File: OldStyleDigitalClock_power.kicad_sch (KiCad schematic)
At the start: 23 parts, among them J1 USB_C_IN, J2 USB_A_OUT, J3 USB_A_OUT, U14 NA555P

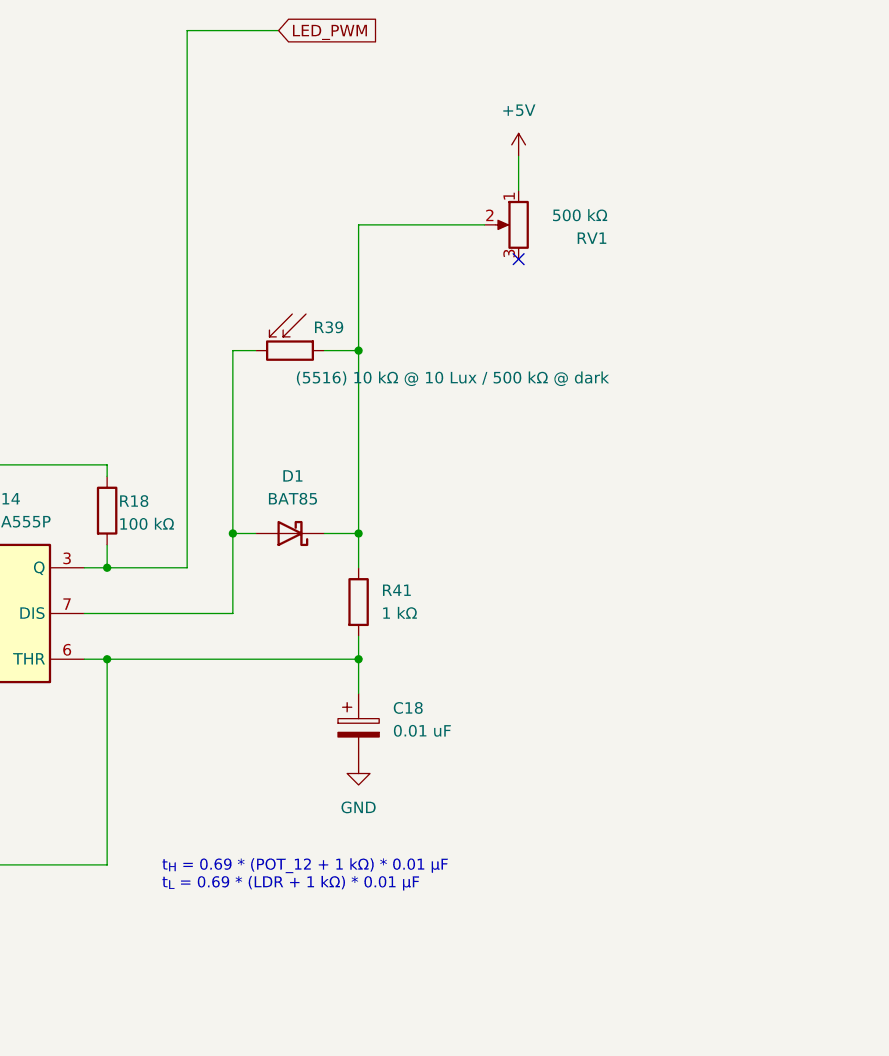
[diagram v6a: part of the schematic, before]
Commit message: Increased C18 value
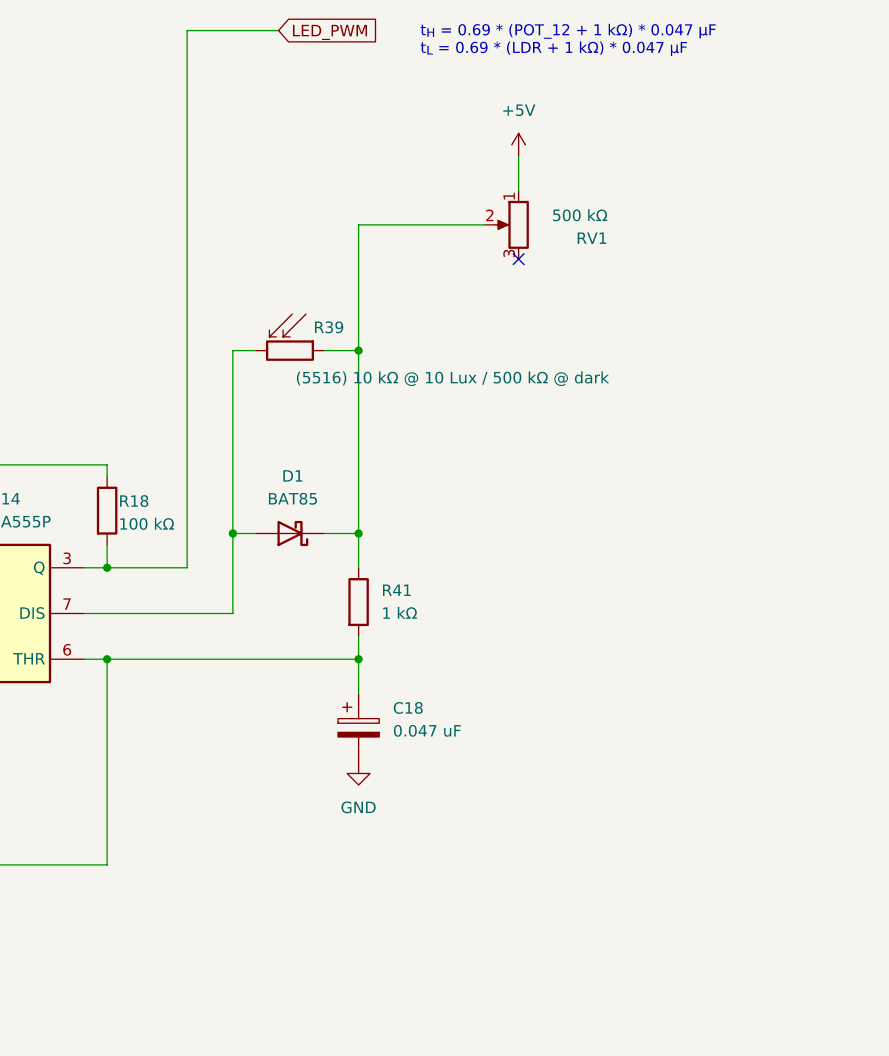
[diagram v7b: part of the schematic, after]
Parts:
- C18: value 0.01 uF -> 0.047 uF
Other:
- note added: "t_{H} = 0.69 * (POT_12 + 1 kΩ) * 0.047 µF t_{L} = 0.69 * (LDR + 1 kΩ) * 0.047 µF"
- note removed: "t_{H} = 0.69 * (POT_12 + 1 kΩ) * 0.01 µF t_{L} = 0.69 * (LDR + 1 kΩ) * 0.01 µF"
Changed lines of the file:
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@@
 		(company "Pasquale Lafiosca")
 	)
-	(text "t_{H} = 0.69 * (POT_12 + 1 kΩ) * 0.01 µF\nt_{L} = 0.69 * (LDR + 1 kΩ) * 0.01 µF\n\n"
+	(text "t_{H} = 0.69 * (POT_12 + 1 kΩ) * 0.047 µF\nt_{L} = 0.69 * (LDR + 1 kΩ) * 0.047 µF\n\n"
 		(exclude_from_sim no)
-		(at 211.836 111.252 0)
+		(at 240.538 18.542 0)
 		(effects
 			(font
@@
 			)
 		)
-		(property "Value" "0.01 uF"
+		(property "Value" "0.047 uF"
 			(at 237.49 96.9009 0)
 			(effects

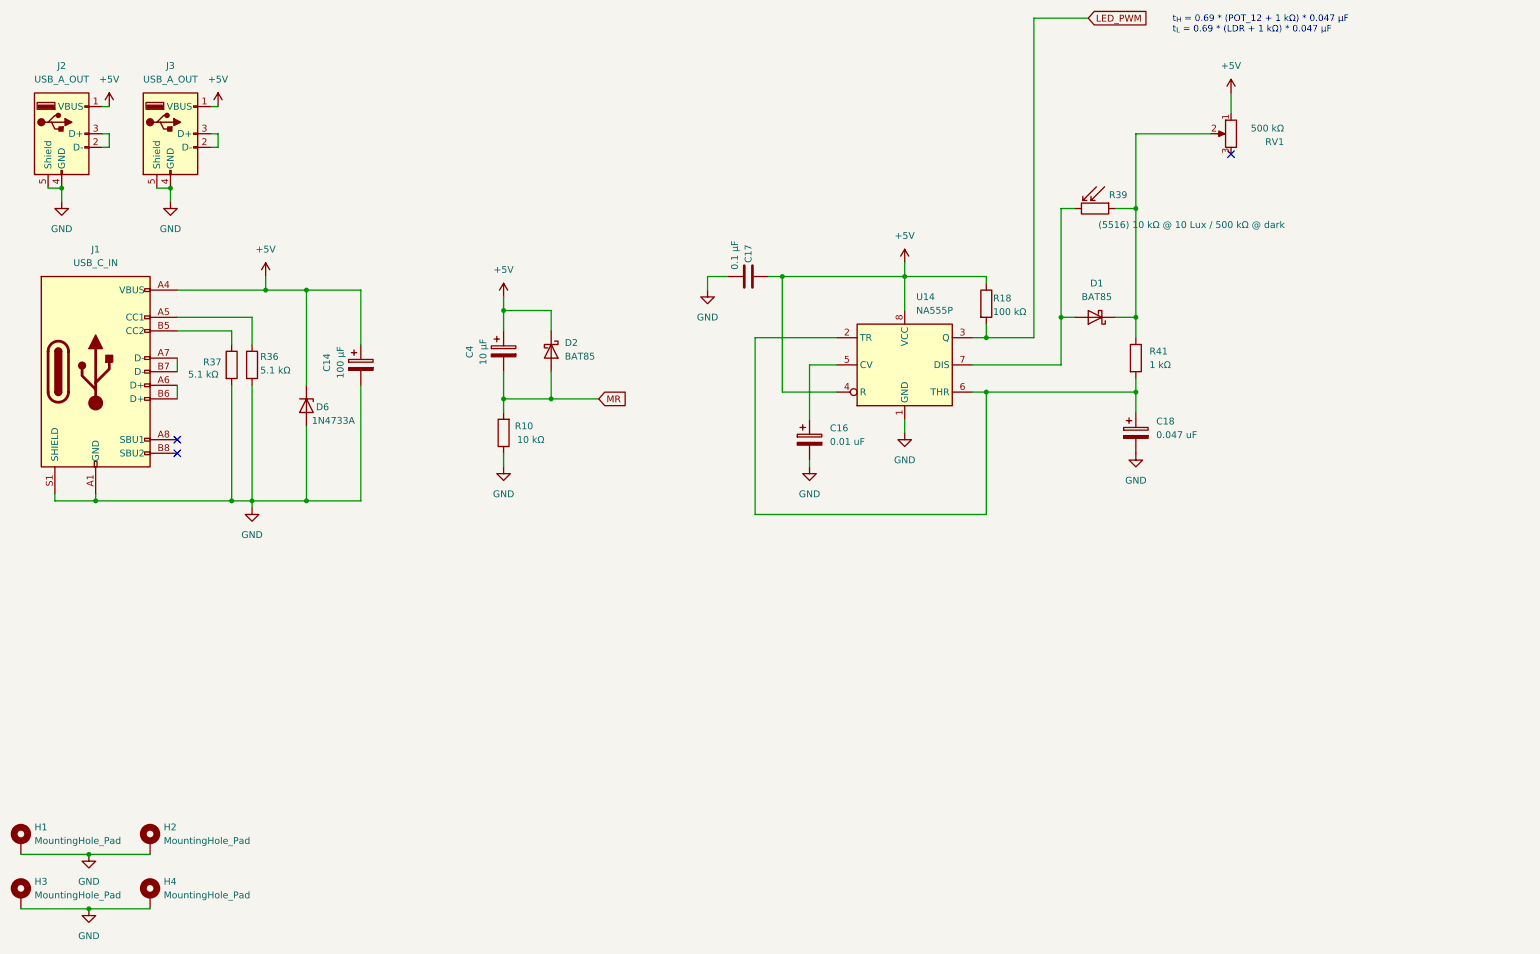
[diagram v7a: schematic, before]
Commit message: Partial commit: Moved to SMD footprints
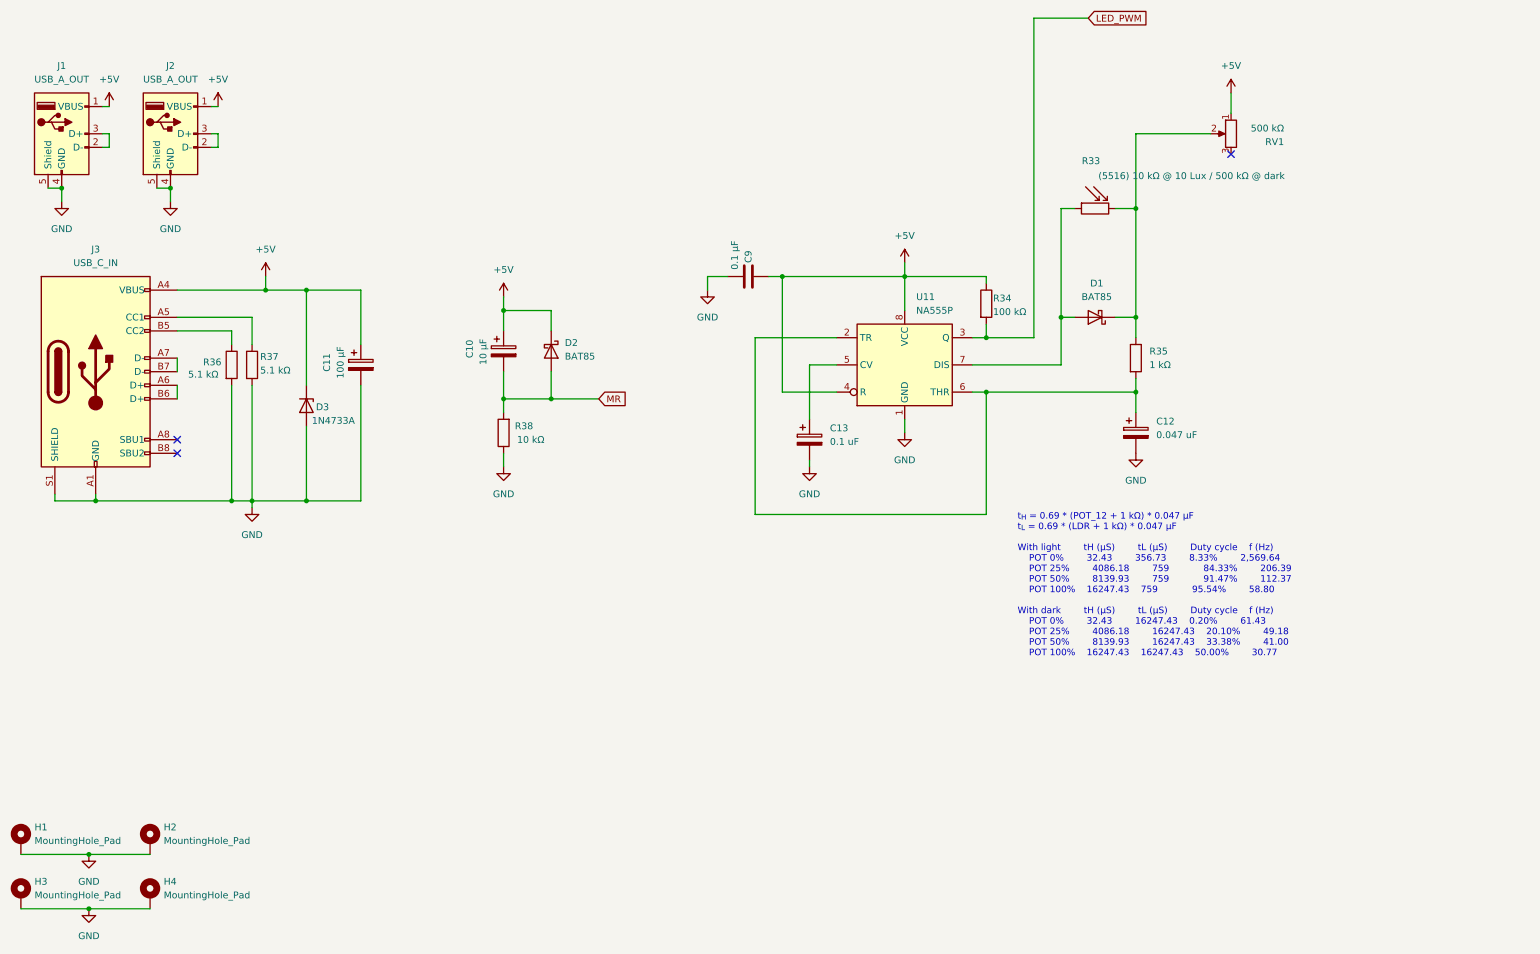
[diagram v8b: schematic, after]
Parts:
- C12: renamed from C18; footprint (none) -> Capacitor_SMD:C_1206_3216Metric
- C13: renamed from C16; value 0.01 uF -> 0.1 uF; footprint (none) -> Capacitor_SMD:C_1206_3216Metric
- C9: renamed from C17; footprint Capacitor_THT:C_Disc_D5.1mm_W3.2mm_P5.00mm -> Capacitor_SMD:C_1206_3216Metric
- R33: renamed from R39; footprint (none) -> OptoDevice:R_LDR_5.1x4.3mm_P3.4mm_Vertical
- R34: renamed from R18; footprint (none) -> Resistor_SMD:R_1206_3216Metric
- R35: renamed from R41; footprint (none) -> Resistor_SMD:R_1206_3216Metric
- R36: renamed from R37; footprint Resistor_THT:R_Axial_DIN0204_L3.6mm_D1.6mm_P7.62mm_Horizontal -> Resistor_SMD:R_1206_3216Metric
- R37: renamed from R36; footprint Resistor_THT:R_Axial_DIN0204_L3.6mm_D1.6mm_P7.62mm_Horizontal -> Resistor_SMD:R_1206_3216Metric
- R38: renamed from R10; footprint Resistor_THT:R_Axial_DIN0204_L3.6mm_D1.6mm_P7.62mm_Horizontal -> Resistor_SMD:R_1206_3216Metric
- RV1: footprint (none) -> Resistor_SMD:R_1206_3216Metric
- renumbered C4 to C10, C14 to C11, D6 to D3, J2 to J1, J3 to J2, J1 to J3, U14 to U11
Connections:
- net at D1.1 (K), R35.1, RV1.2: now also R33.2; no longer R33.1
- net at D1.2 (A), U11.7 (DIS): now also R33.1; no longer R33.2
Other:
- note added: "t_{H} = 0.69 * (POT_12 + 1 kΩ) * 0.047 µF t_{L} = 0.69 * (LDR + 1 kΩ) * 0.047 µF With light tH (µS) tL (µS) Duty cycle f (Hz) POT 0% 32.43 356.73 8.33% 2,569.64 POT 25% 4086.18 759 84.33% 206.39 POT 50% 8139.93 759 91.47% 112.37 POT 100% 16247.43 759 95.54% 58.80 With dark tH (µS) tL (µS) Duty cycle f (Hz) POT 0% 32.43 16247.43 0.20% 61.43 POT 25% 4086.18 16247.43 20.10% 49.18 POT 50% 8139.93 162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"
- note removed: "t_{H} = 0.69 * (POT_12 + 1 kΩ) * 0.047 µF t_{L} = 0.69 * (LDR + 1 kΩ) * 0.047 µF"
- moved on the sheet: R33
